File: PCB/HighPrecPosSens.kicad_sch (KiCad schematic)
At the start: 69 parts

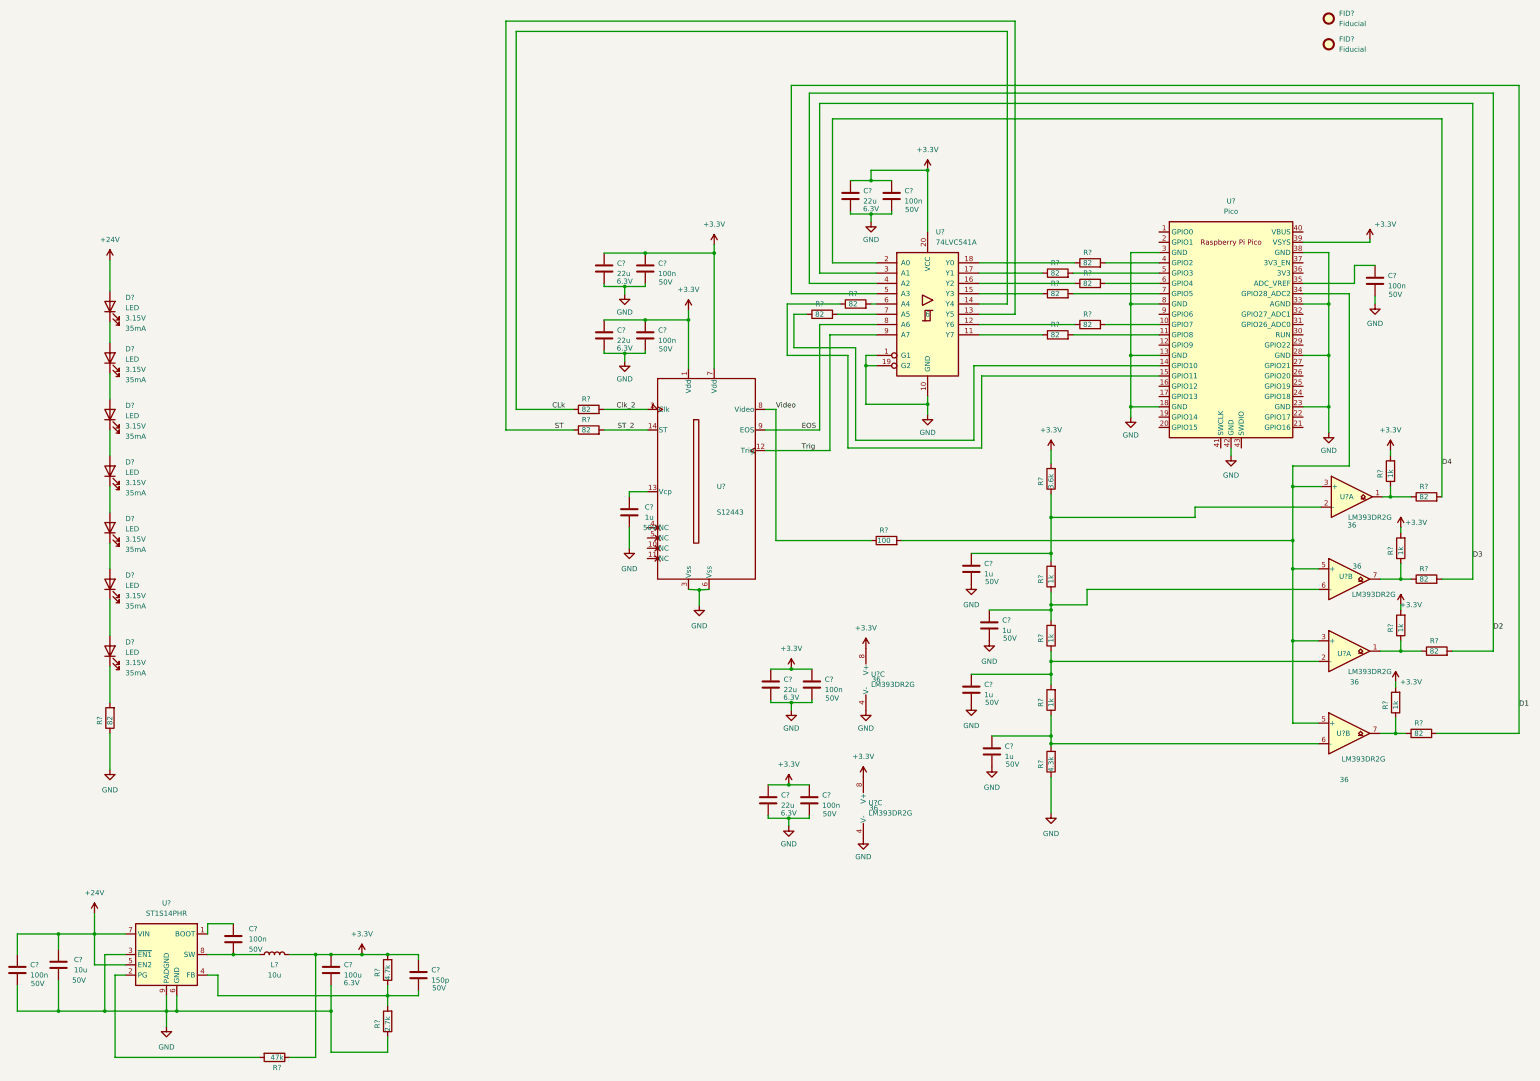
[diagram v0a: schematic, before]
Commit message: First netlist transfer
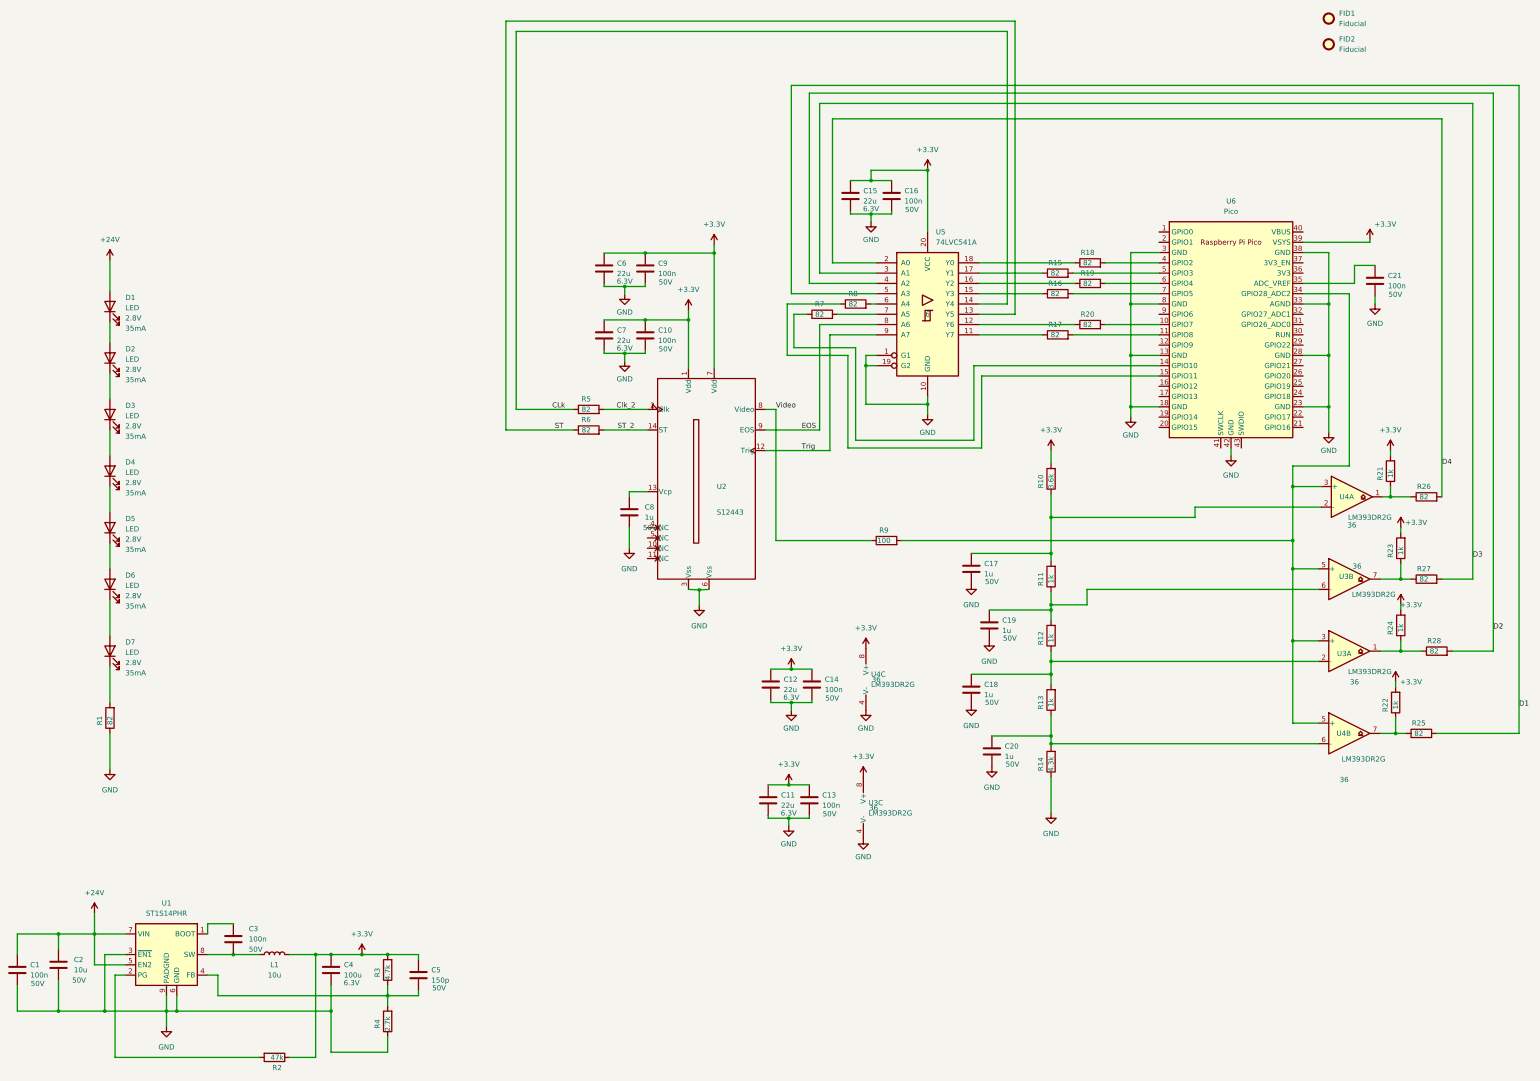
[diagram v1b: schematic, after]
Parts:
- D1, D2, D3, D4, D5, D6, D7: renamed from D?; footprint (none) -> LED_SMD:LED_0603_1608Metric_Pad1.05x0.95mm_HandSolder; Manufacturer (none) -> Everlight; ManufacturerPartNum (none) -> 19-217/BHC-ZL1M2RY/3T; SourcingPartNum (none) -> C72041; Umax 3.15V -> 2.8V
- gave numbers to parts that had none: 58

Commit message: Some layouting
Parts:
- renumbered U4 to U3, U3 to U4
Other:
- moved on the sheet: U4A
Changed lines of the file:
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@@
     (stroke (width 0) (type default) (color 0 0 0 0))
   )
-  (wire (pts (xy 336.55 170.18) (xy 342.9 170.18))
+  (wire (pts (xy 336.55 170.18) (xy 344.424 170.18))
     (stroke (width 0) (type default) (color 0 0 0 0))
   )
-  (wire (pts (xy 358.14 172.72) (xy 363.22 172.72))
+  (wire (pts (xy 359.664 172.72) (xy 363.22 172.72))
     (stroke (width 0) (type default) (color 0 0 0 0))
   )
@@
     (stroke (width 0) (type default) (color 0 0 0 0))
   )
-  (wire (pts (xy 276.86 175.26) (xy 342.9 175.26))
+  (wire (pts (xy 276.86 175.26) (xy 344.424 175.26))
     (stroke (width 0) (type default) (color 0 0 0 0))
   )
@@
   (symbol (lib_id "Comparator:LM393") (at 351.155 134.62 0) (unit 1)
     (in_bom yes) (on_board yes)
-    (property "Reference" "U4" (id 0) (at 349.885 134.62 0))
+    (property "Reference" "U3" (id 0) (at 349.885 134.62 0))
     (property "Value" "LM393DR2G" (id 1) (at 355.6 139.7 0))
     (property "Footprint" "Package_SO:SOIC-8_3.9x4.9mm_P1.27mm" (id 2) (at 351.155 134.62 0)
@@
     (pin "2")
   )
-  (symbol (lib_id "Comparator:LM393") (at 350.52 172.72 0) (unit 1)
+  (symbol (lib_id "Comparator:LM393") (at 352.044 172.72 0) (unit 1)
     (in_bom yes) (on_board yes)
-    (property "Reference" "U3" (id 0) (at 349.25 173.355 0))
-    (property "Value" "LM393DR2G" (id 1) (at 355.6 177.8 0))
-    (property "Footprint" "Package_SO:SOIC-8_3.9x4.9mm_P1.27mm" (id 2) (at 350.52 172.72 0)
+    (property "Reference" "U4" (id 0) (at 350.774 173.355 0))
+    (property "Value" "LM393DR2G" (id 1) (at 357.124 177.8 0))
+    (property "Footprint" "Package_SO:SOIC-8_3.9x4.9mm_P1.27mm" (id 2) (at 352.044 172.72 0)
       (effects (font (size 1.27 1.27)) hide)
     )
-    (property "Datasheet" "http://www.ti.com/lit/ds/symlink/lm393.pdf" (id 3) (at 350.52 172.72 0)
+    (property "Datasheet" "http://www.ti.com/lit/ds/symlink/lm393.pdf" (id 3) (at 352.044 172.72 0)
       (effects (font (size 1.27 1.27)) hide)
     )
-    (property "Manufacturer" "onsemi" (id 4) (at 350.52 172.72 0)
+    (property "Manufacturer" "onsemi" (id 4) (at 352.044 172.72 0)
       (effects (font (size 1.27 1.27)) hide)
     )
-    (property "ManufacturerPartNum" "LM393DR2G" (id 5) (at 350.52 172.72 0)
+    (property "ManufacturerPartNum" "LM393DR2G" (id 5) (at 352.044 172.72 0)
       (effects (font (size 1.27 1.27)) hide)
     )
-    (property "Sourcing" "JLCPCB" (id 6) (at 350.52 172.72 0)
+    (property "Sourcing" "JLCPCB" (id 6) (at 352.044 172.72 0)
       (effects (font (size 1.27 1.27)) hide)
     )
-    (property "SourcingPartNum" "C7955" (id 7) (at 350.52 172.72 0)
+    (property "SourcingPartNum" "C7955" (id 7) (at 352.044 172.72 0)
       (effects (font (size 1.27 1.27)) hide)
     )
-    (property "Umax" "36" (id 8) (at 351.79 180.34 0))
+    (property "Umax" "36" (id 8) (at 353.314 180.34 0))
     (pin "1")
     (pin "2")
@@
       (reference "U2") (unit 1) (value "S12443") (footprint "SensorLibrary:s12443")
     )
-    (path "/55e111bf-27bd-489a-901e-36acc2c2055b"
+    (path "/48dc9315-17f7-412f-8df9-391b1b372a02"
       (reference "U3") (unit 1) (value "LM393DR2G") (footprint "Package_SO:SOIC-8_3.9x4.9mm_P1.27mm")
     )
@@
       (reference "U3") (unit 3) (value "LM393DR2G") (footprint "Package_SO:SOIC-8_3.9x4.9mm_P1.27mm")
     )
-    (path "/48dc9315-17f7-412f-8df9-391b1b372a02"
+    (path "/55e111bf-27bd-489a-901e-36acc2c2055b"
       (reference "U4") (unit 1) (value "LM393DR2G") (footprint "Package_SO:SOIC-8_3.9x4.9mm_P1.27mm")
     )

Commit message: layouting
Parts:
- added D8: SS36, Diode_SMD:D_SMC_Handsoldering, symbol Device:D_Schottky_Filled
- added J1, J2, J3, J4: Conn_01x02_Male, Connector_PinHeader_2.54mm:PinHeader_1x02_P2.54mm_Vertical, symbol Connector:Conn_01x02_Male
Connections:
- net GND: now also D8.2 (A)
- net V1: now reaches C20.1, R13.1, R14.2, U4.6 (-)
- net PGood: now reaches R2.2, U1.2 (PG)
- net PGood: now also U6.20 (GPIO15)
- net at C3.2, L1.1, U1.8 (SW): now also D8.1 (K)
- net V2: now reaches C18.1, R12.1, R13.2, U4.2 (-)
- net V4: now reaches R9.2, U3.3 (+), U3.5 (+), U4.3 (+), U4.5 (+), U6.34 (GPIO28_ADC2)
- net V3: now reaches C19.1, R11.1, R12.2, U3.6 (-)

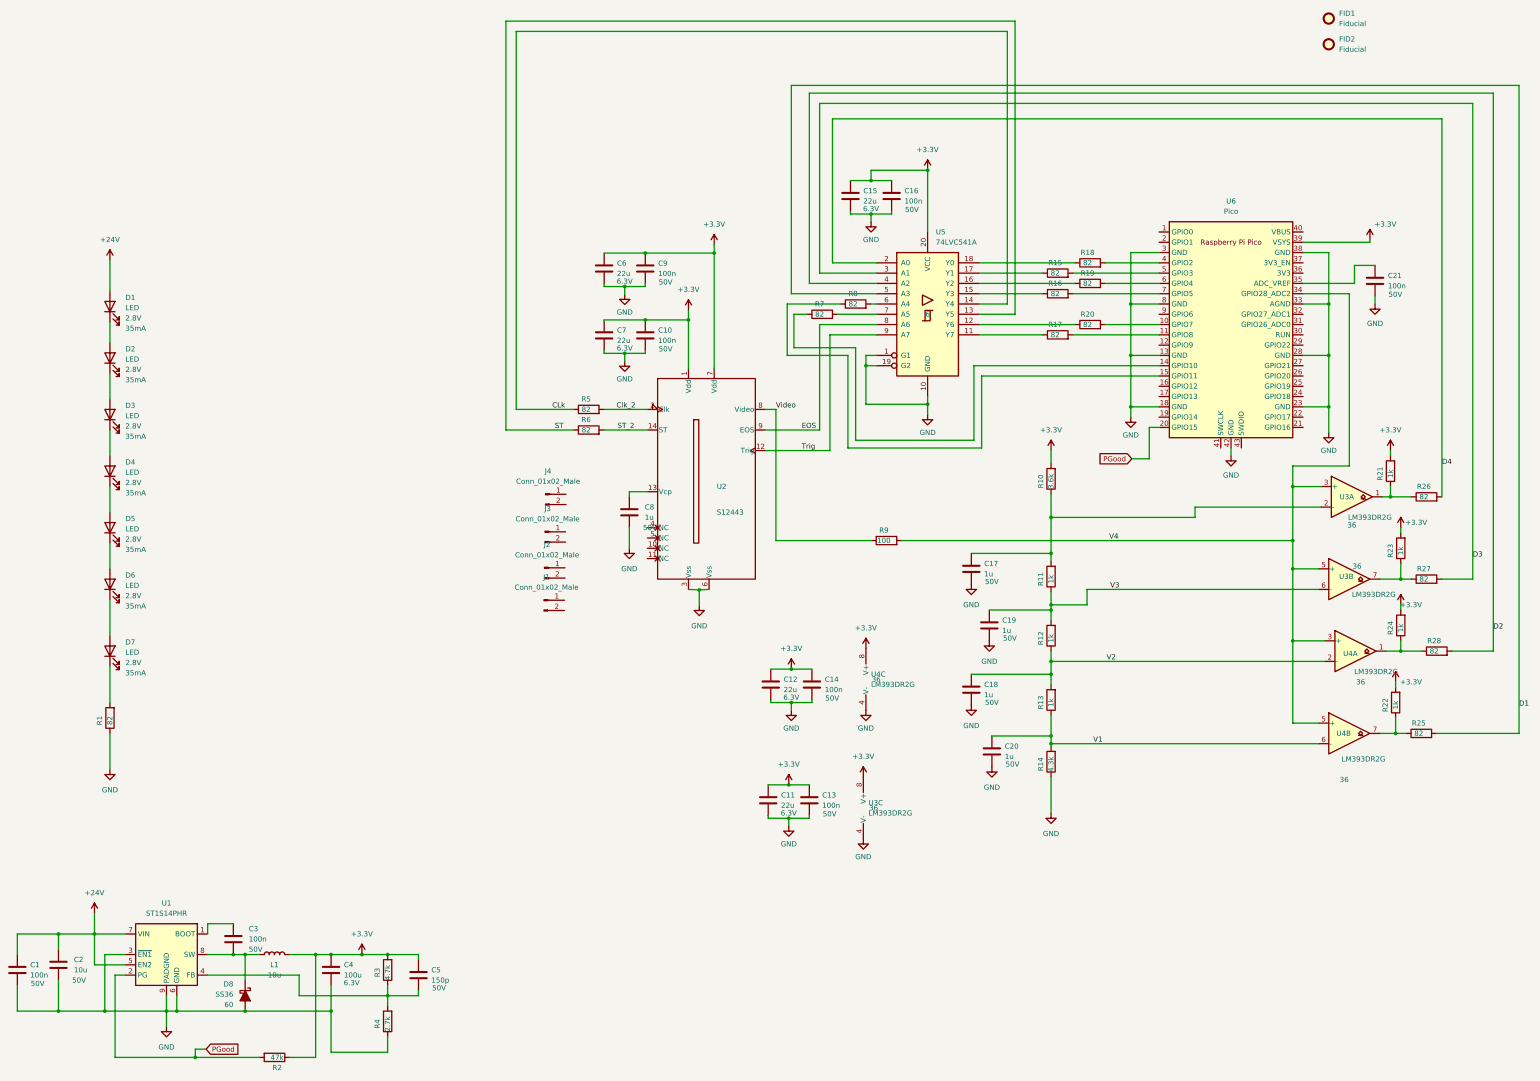
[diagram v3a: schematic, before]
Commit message: Added some missing parts and more LEDs
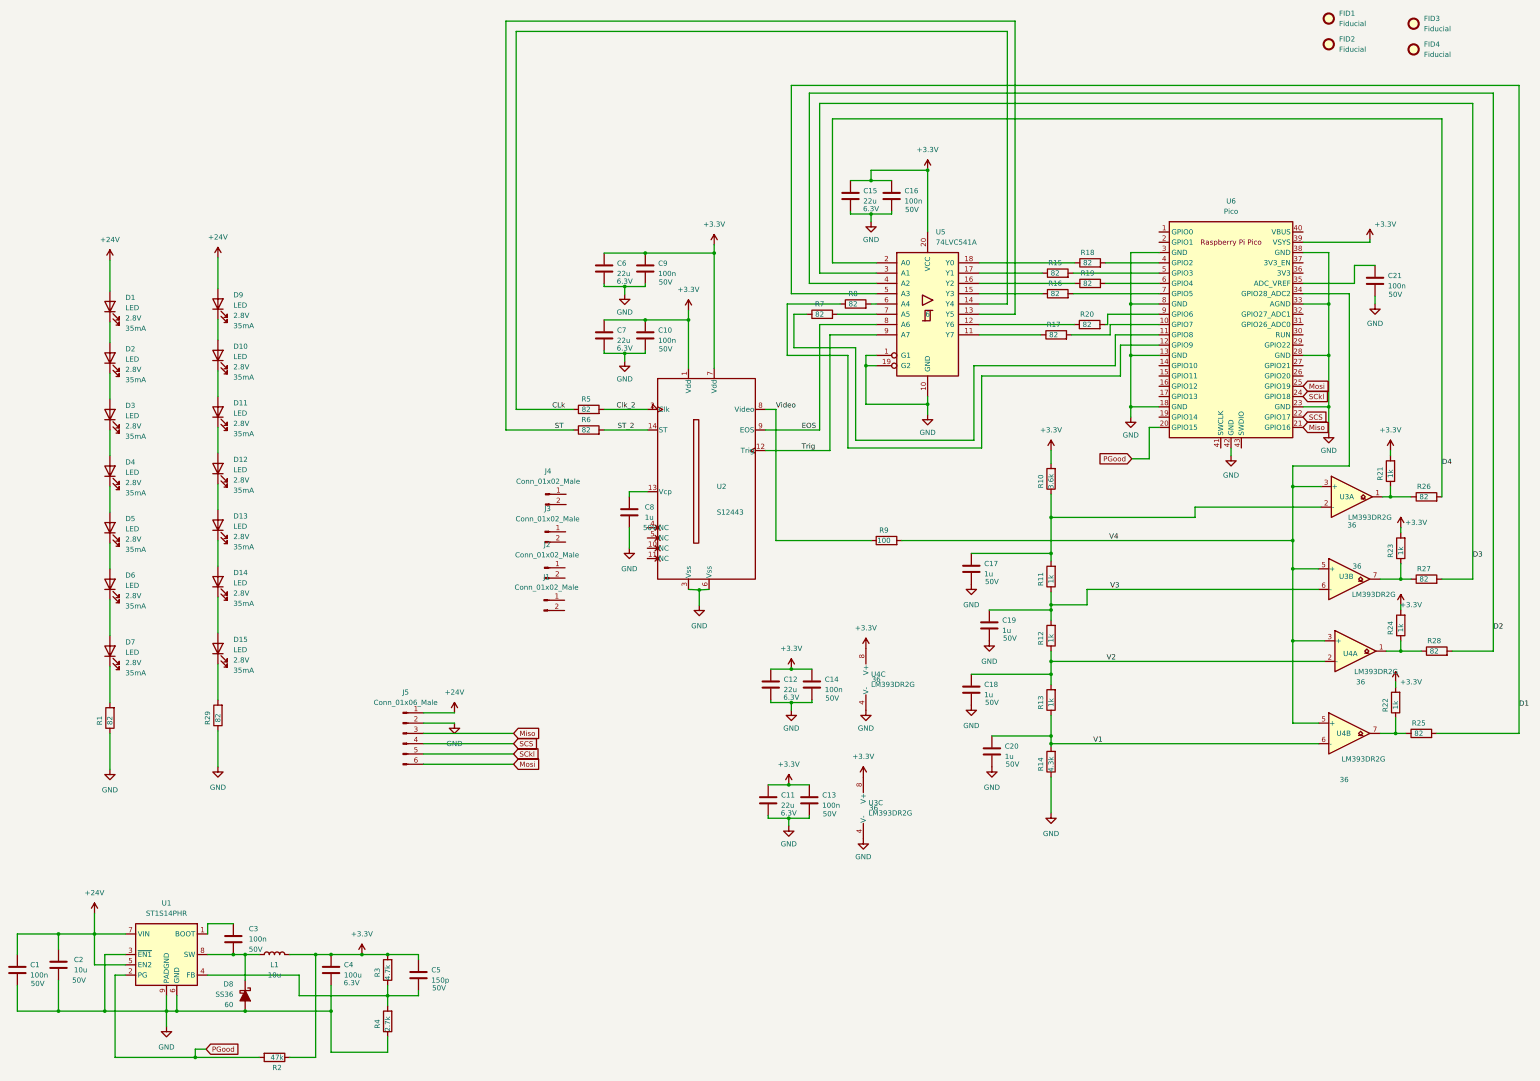
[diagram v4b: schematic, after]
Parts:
- added D10, D11, D12, D13, D14, D15, D9: LED, LED_SMD:LED_0603_1608Metric_Pad1.05x0.95mm_HandSolder, symbol Device:LED
- added FID3, FID4: Fiducial, Fiducial:Fiducial_1mm_Mask2mm, symbol Mechanical:Fiducial
- added J5: Conn_01x06_Male, Connector_JST:JST_XH_B6B-XH-A_1x06_P2.50mm_Vertical, symbol Connector:Conn_01x06_Male
- added R29: 82, Resistor_SMD:R_0603_1608Metric, symbol Device:R
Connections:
- net +24V: now also D9.2 (A), J5.1 (Pin_1)
- net GND: now also J5.2 (Pin_2), R29.1
- net at R20.2: now also U6.9 (GPIO6); no longer U6.10 (GPIO7)
- net at R17.2: now also U6.10 (GPIO7); no longer U6.11 (GPIO8)
- net at U6.12 (GPIO9): now also R8.1
- net at R7.1: now also U6.11 (GPIO8); no longer U6.14 (GPIO10)
- net at U6.15 (GPIO11): no longer R8.1
- net Miso: now reaches U6.21 (GPIO16)
- net Miso: now also J5.3 (Pin_3)
- net SCS: now reaches U6.22 (GPIO17)
- net SCS: now also J5.4 (Pin_4)
- net SCkl: now reaches U6.24 (GPIO18)
- net SCkl: now also J5.5 (Pin_5)
- net Mosi: now reaches U6.25 (GPIO19)
- net Mosi: now also J5.6 (Pin_6)
- new net: D12.1 (K), D13.2 (A)
- new net: D11.1 (K), D12.2 (A)
- new net: D10.1 (K), D11.2 (A)
- new net: D10.2 (A), D9.1 (K)
- new net: D14.1 (K), D15.2 (A)
- new net: D13.1 (K), D14.2 (A)
- new net: D15.1 (K), R29.2

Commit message: Routed layout
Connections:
- net V4: now also C17.1, R10.1, R11.2, U3.2 (-); no longer R9.2, U3.3 (+), U3.5 (+), U4.3 (+), U4.5 (+), U6.34 (GPIO28_ADC2)
- net Boot: now reaches C3.1, U1.1 (BOOT)
- net FB: now reaches C5.2, R3.1, R4.2, U1.4 (FB)
- net Switch: now reaches C3.2, D8.1 (K), L1.1, U1.8 (SW)
- new net Video1: R9.2, U3.3 (+), U3.5 (+), U4.3 (+), U4.5 (+), U6.34 (GPIO28_ADC2)
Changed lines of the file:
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@@
+    (effects (font (size 1.27 1.27)) (justify left bottom))
+  )
+  (label "Switch" (at 69.85 247.65 0)
+    (effects (font (size 1.27 1.27)) (justify left bottom))
+  )
+  (label "FB" (at 89.535 252.73 0)
+    (effects (font (size 1.27 1.27)) (justify left bottom))
+  )
+  (label "Video1" (at 301.625 145.415 0)
     (effects (font (size 1.27 1.27)) (justify left bottom))
   )
@@
     (effects (font (size 1.27 1.27)) (justify left bottom))
   )
-  (label "V4" (at 291.211 145.415 0)
+  (label "V4" (at 294.005 139.7 0)
     (effects (font (size 1.27 1.27)) (justify left bottom))
   )
+  (label "Boot" (at 72.39 240.03 0)
+    (effects (font (size 1.27 1.27)) (justify left bottom))
+  )
